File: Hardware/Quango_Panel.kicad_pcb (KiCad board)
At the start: 2 copper layers, 81 x 128.5 mm, 30 parts

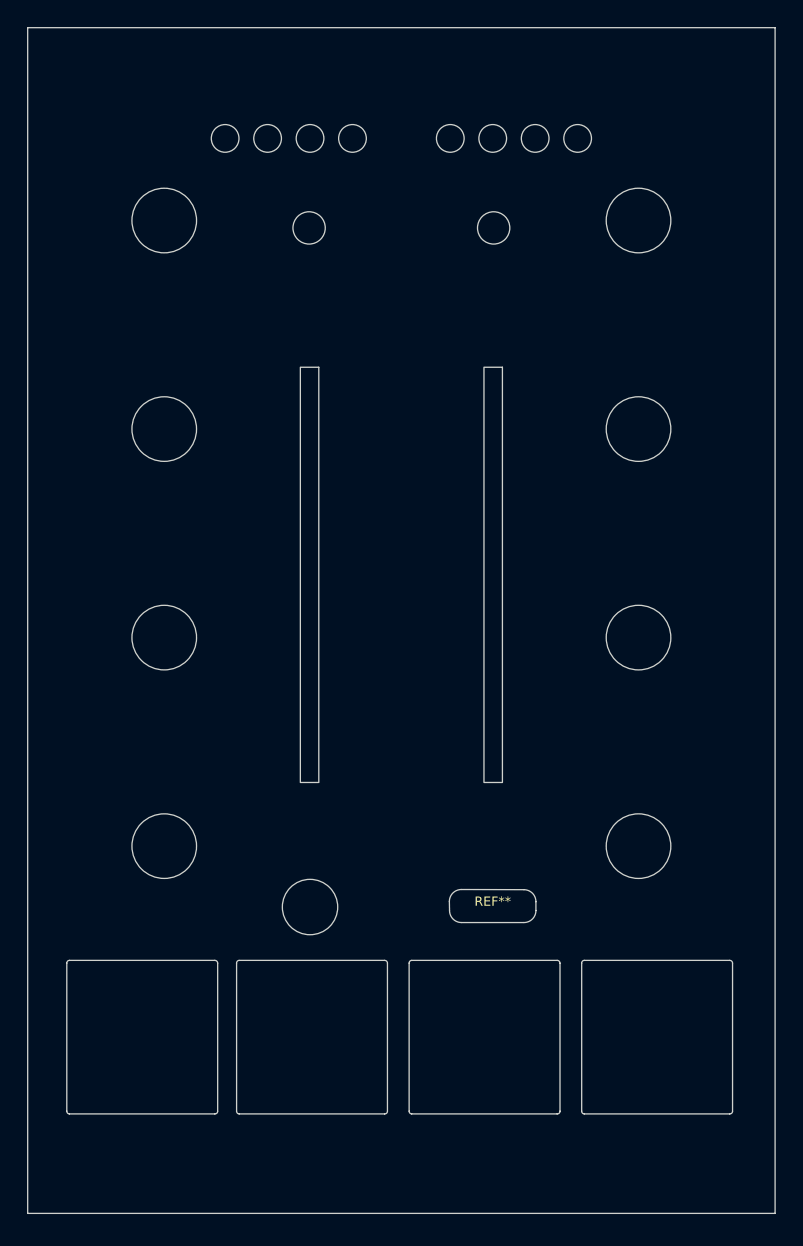
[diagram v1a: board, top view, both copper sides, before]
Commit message: Clean Up of Panel and Control boards
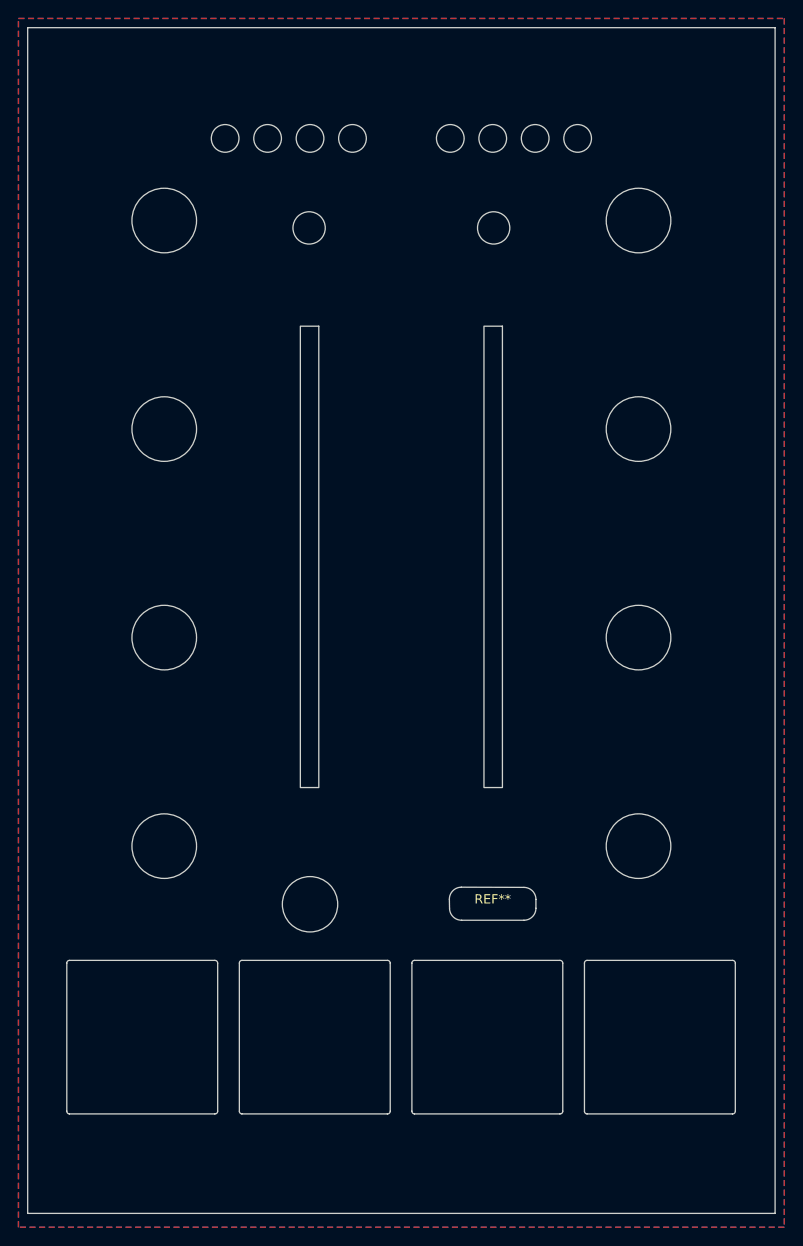
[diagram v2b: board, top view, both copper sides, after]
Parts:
- added G***: LOGO, Graphics:QuangoLogo, F.Cu at (90.5, 34.5)
- added kibuzzard-646A4A79: G***, kibuzzard-646A4A79, F.Cu at (53.7, 51.0)
- added kibuzzard-646A4AA7: G***, kibuzzard-646A4AA7, F.Cu at (53.6, 118.7)
- added kibuzzard-646A4AAE: G***, kibuzzard-646A4AAE, F.Cu at (53.5, 96.1)
- added kibuzzard-646A4AB4: G***, kibuzzard-646A4AB4, F.Cu at (53.6, 73.7)
- added kibuzzard-646A4AD3: G***, kibuzzard-646A4AD3, F.Cu at (127.5, 50.8)
- added kibuzzard-646A4ADD: G***, kibuzzard-646A4ADD, F.Cu at (127.4, 73.5)
- added kibuzzard-646A4AF1: G***, kibuzzard-646A4AF1, F.Cu at (127.3, 95.9)
- added kibuzzard-646A4AF9: G***, kibuzzard-646A4AF9, F.Cu at (127.4, 118.5)
- added kibuzzard-646A4B72: G***, kibuzzard-646A4B72, F.Cu at (90.2, 125.0)
- added kibuzzard-646A4B84: G***, kibuzzard-646A4B84, F.Cu at (90.5, 51.7)
- added kibuzzard-646A4E06: G***, kibuzzard-646A4E06, F.Cu at (62.4, 150.2)
- added kibuzzard-646A4E18: G***, kibuzzard-646A4E18, F.Cu at (118.5, 150.2)
- added kibuzzard-646A4E25: G***, kibuzzard-646A4E25, F.Cu at (99.8, 150.2)
- added kibuzzard-646A4E4E: G***, kibuzzard-646A4E4E, F.Cu at (81.1, 150.2)
- moved Level1 1.95 mm to (82.3, 58.1)
- moved Level1 1.95 mm to (102.2, 58.1)
- moved REF** 0.30 mm to (99.8, 139.4)
- moved REF** 0.30 mm to (118.5, 139.4)
- moved REF** 0.30 mm to (81.1, 139.4)
- moved Ref** 0.30 mm to (80.6, 125.0)
- moved REF** 0.25 mm to (100.4, 125.0)
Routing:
- added copper zone on B.Cu, net (none)
- added copper zone on F.Cu, net (none)
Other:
- board text added: "JLCJLCJLCJLC"
- board text added: "Mountjoy Modular 2023 Quango Panel v1.0"

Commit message: Set up JLC parts placement details
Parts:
- removed kibuzzard-646A4A79: G***, kibuzzard-646A4A79
- removed kibuzzard-646A4AA7: G***, kibuzzard-646A4AA7
- removed kibuzzard-646A4AAE: G***, kibuzzard-646A4AAE
- removed kibuzzard-646A4AB4: G***, kibuzzard-646A4AB4
- removed kibuzzard-646A4B72: G***, kibuzzard-646A4B72
- removed kibuzzard-646A4B84: G***, kibuzzard-646A4B84
- added kibuzzard-646B3A7F: G***, kibuzzard-646B3A7F, F.Cu at (90.5, 51.7)
- added kibuzzard-646B3DF5: G***, kibuzzard-646B3DF5, F.Cu at (90.2, 125.0)
- added kibuzzard-646B76FE: G***, kibuzzard-646B76FE, F.Cu at (53.7, 51.0)
- added kibuzzard-646B7712: G***, kibuzzard-646B7712, F.Cu at (53.4, 73.7)
- added kibuzzard-646B771E: G***, kibuzzard-646B771E, F.Cu at (53.4, 118.7)
- added kibuzzard-646B781D: G***, kibuzzard-646B781D, F.Cu at (53.9, 96.1)

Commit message: Updates to Panel Graphics
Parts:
- removed kibuzzard-646A4AF1: G***, kibuzzard-646A4AF1
- removed kibuzzard-646A4E06: G***, kibuzzard-646A4E06
- removed kibuzzard-646A4E18: G***, kibuzzard-646A4E18
- removed kibuzzard-646A4E25: G***, kibuzzard-646A4E25
- removed kibuzzard-646A4E4E: G***, kibuzzard-646A4E4E
- removed kibuzzard-646B3A7F: G***, kibuzzard-646B3A7F
- removed kibuzzard-646B3DF5: G***, kibuzzard-646B3DF5
- removed kibuzzard-646B781D: G***, kibuzzard-646B781D
- added kibuzzard-646B9F04: G***, kibuzzard-646B9F04, F.Cu at (90.5, 124.4)
- added kibuzzard-646B9FB5: G***, kibuzzard-646B9FB5, F.Cu at (53.9, 96.1)
- added kibuzzard-646BA02D: G***, kibuzzard-646BA02D, F.Cu at (127.0, 95.9)
- added kibuzzard-646BA165: G***, kibuzzard-646BA165, F.Cu at (90.5, 51.7)
- added kibuzzard-646BA8C3: G***, kibuzzard-646BA8C3, F.Cu at (82.2, 150.2)
- added kibuzzard-646BA8CA: G***, kibuzzard-646BA8CA, F.Cu at (98.8, 150.2)
- moved kibuzzard-646B7712 73.6 mm to (127.0, 73.6)
- moved kibuzzard-646B771E 73.6 mm to (127.0, 118.6)
- moved kibuzzard-646A4ADD 73.4 mm to (54.0, 73.5)
- moved kibuzzard-646A4AF9 73.4 mm to (54.0, 118.5)
- moved kibuzzard-646A4AD3 73.2 mm to (54.3, 50.8)
- moved kibuzzard-646B76FE 73.0 mm to (126.7, 50.9)
- moved REF** 0.75 mm to (100.4, 124.2)
- moved Ref** 0.70 mm to (80.6, 124.3)
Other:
- board text added: "CV A"
- board text added: "CV B"
- board text added: "Mountjoy Modular"

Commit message: Final Updates for v1.0 production
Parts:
- removed kibuzzard-646A4AD3: G***, kibuzzard-646A4AD3
- removed kibuzzard-646A4ADD: G***, kibuzzard-646A4ADD
- removed kibuzzard-646A4AF9: G***, kibuzzard-646A4AF9
- removed kibuzzard-646B76FE: G***, kibuzzard-646B76FE
- removed kibuzzard-646B7712: G***, kibuzzard-646B7712
- removed kibuzzard-646B771E: G***, kibuzzard-646B771E
- removed kibuzzard-646B9F04: G***, kibuzzard-646B9F04
- removed kibuzzard-646B9FB5: G***, kibuzzard-646B9FB5
- removed kibuzzard-646BA02D: G***, kibuzzard-646BA02D
- added kibuzzard-646C865B: G***, kibuzzard-646C865B, F.Cu at (90.5, 124.4)
- added kibuzzard-646C8A92: G***, kibuzzard-646C8A92, F.Cu at (54.3, 96.1)
- added kibuzzard-646C8AA8: G***, kibuzzard-646C8AA8, F.Cu at (54.3, 73.4)
- added kibuzzard-646C8AB8: G***, kibuzzard-646C8AB8, F.Cu at (54.3, 118.5)
- added kibuzzard-646C8AC0: G***, kibuzzard-646C8AC0, F.Cu at (54.6, 50.8)
- added kibuzzard-646C8AF5: G***, kibuzzard-646C8AF5, F.Cu at (126.2, 50.9)
- added kibuzzard-646C8AFB: G***, kibuzzard-646C8AFB, F.Cu at (126.5, 73.6)
- added kibuzzard-646C8B02: G***, kibuzzard-646C8B02, F.Cu at (126.5, 95.9)
- added kibuzzard-646C8B09: G***, kibuzzard-646C8B09, F.Cu at (126.5, 118.6)
- moved kibuzzard-646BA8C3 0.40 mm to (82.2, 150.6)
- moved kibuzzard-646BA8CA 0.40 mm to (98.8, 150.6)

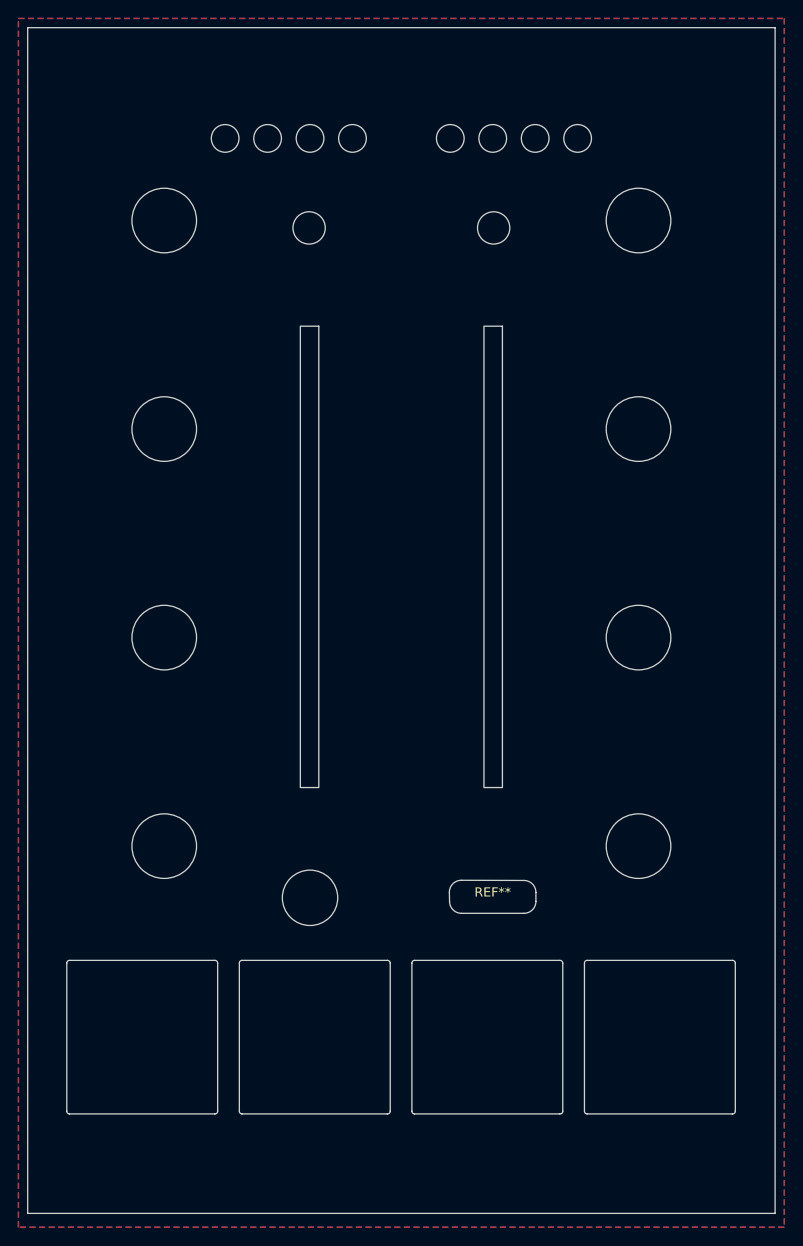
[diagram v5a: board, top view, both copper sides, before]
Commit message: Updated controls to include octave switching; revised panel
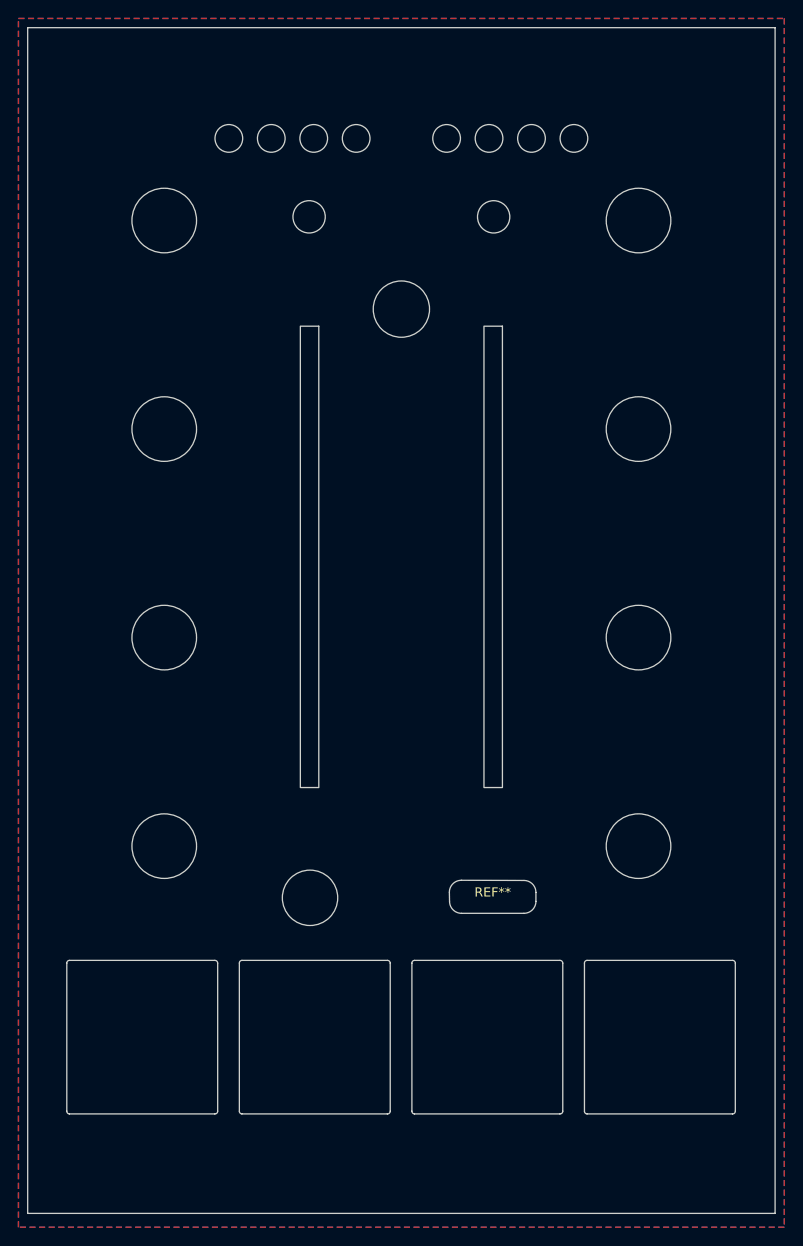
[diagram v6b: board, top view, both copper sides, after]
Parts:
- removed kibuzzard-646BA8C3: G***, kibuzzard-646BA8C3
- removed kibuzzard-646BA8CA: G***, kibuzzard-646BA8CA
- removed kibuzzard-646C8A92: G***, kibuzzard-646C8A92
- removed kibuzzard-646C8AA8: G***, kibuzzard-646C8AA8
- removed kibuzzard-646C8AB8: G***, kibuzzard-646C8AB8
- removed kibuzzard-646C8AC0: G***, kibuzzard-646C8AC0
- removed kibuzzard-646C8AF5: G***, kibuzzard-646C8AF5
- removed kibuzzard-646C8AFB: G***, kibuzzard-646C8AFB
- removed kibuzzard-646C8B02: G***, kibuzzard-646C8B02
- removed kibuzzard-646C8B09: G***, kibuzzard-646C8B09
- added Ref**: Thonkikonn_6.1mm, Custom_Footprints:MountingHole_6.1mm, F.Cu at (90.5, 60.5)
- added kibuzzard-649D9A54: G***, kibuzzard-649D9A54, F.Cu at (60.1, 150.6)
- added kibuzzard-649D9A54: G***, kibuzzard-649D9A54, F.Cu at (115.7, 150.6)
- added kibuzzard-649D9A6F: G***, kibuzzard-649D9A6F, F.Cu at (98.6, 150.6)
- added kibuzzard-649D9B19: G***, kibuzzard-649D9B19, F.Cu at (54.8, 50.7)
- added kibuzzard-649D9B1E: G***, kibuzzard-649D9B1E, F.Cu at (54.5, 73.3)
- added kibuzzard-649D9B25: G***, kibuzzard-649D9B25, F.Cu at (54.5, 96.0)
- added kibuzzard-649D9B2C: G***, kibuzzard-649D9B2C, F.Cu at (54.5, 118.4)
- added kibuzzard-649D9B57: G***, kibuzzard-649D9B57, F.Cu at (126.2, 50.9)
- added kibuzzard-649D9B5F: G***, kibuzzard-649D9B5F, F.Cu at (126.5, 73.6)
- added kibuzzard-649D9B68: G***, kibuzzard-649D9B68, F.Cu at (126.5, 95.9)
- added kibuzzard-649D9B6F: G***, kibuzzard-649D9B6F, F.Cu at (126.5, 118.6)
- added kibuzzard-649DB4CB: G***, kibuzzard-649DB4CB, F.Cu at (90.4, 71.2)
- added kibuzzard-649DB643: G***, kibuzzard-649DB643, F.Cu at (82.5, 150.6)
- moved RESET 1.20 mm to (80.5, 50.5)
- moved RESET 1.20 mm to (100.5, 50.5)
- moved kibuzzard-646BA165 1.20 mm to (90.5, 50.5)
- moved Ref** 0.40 mm to (81.0, 42.0)
- moved Ref** 0.40 mm to (104.6, 42.0)
- moved Ref** 0.40 mm to (76.4, 42.0)
- moved Ref** 0.40 mm to (100.0, 42.0)
- moved Ref** 0.40 mm to (71.8, 42.0)
- moved Ref** 0.40 mm to (109.2, 42.0)
- moved Ref** 0.40 mm to (95.4, 42.0)
- moved Ref** 0.40 mm to (85.6, 42.0)
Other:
- board text added: "IN"
- board text added: "Mountjoy Modular 2023 Quango Panel v2.0"
- board text removed: "CV A"
- board text removed: "CV B"
- board text removed: "Mountjoy Modular 2023 Quango Panel v1.0"

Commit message: Prepared v2 controls and panel for  manufacture
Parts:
- removed kibuzzard-649DB4CB: G***, kibuzzard-649DB4CB
- added kibuzzard-649E93AB: G***, kibuzzard-649E93AB, F.Cu at (90.4, 74.9)
